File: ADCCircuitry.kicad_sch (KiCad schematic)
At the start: 16 parts, among them U7 ADS112C04

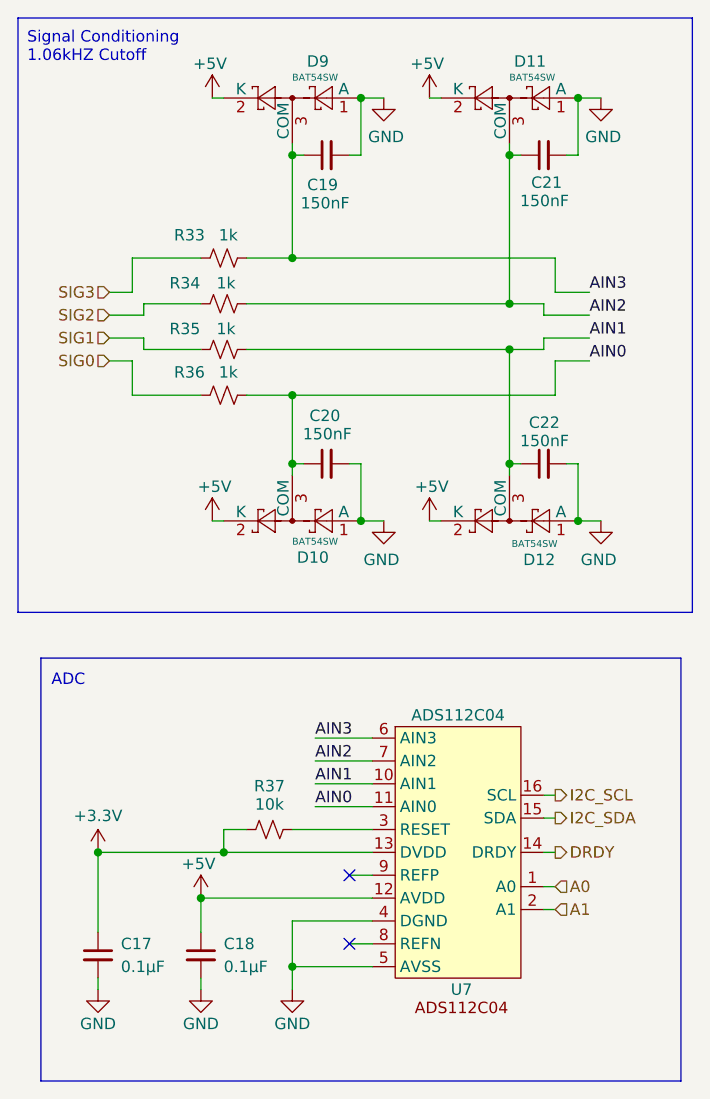
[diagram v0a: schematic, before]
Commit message: add capacitor and resistor footprints
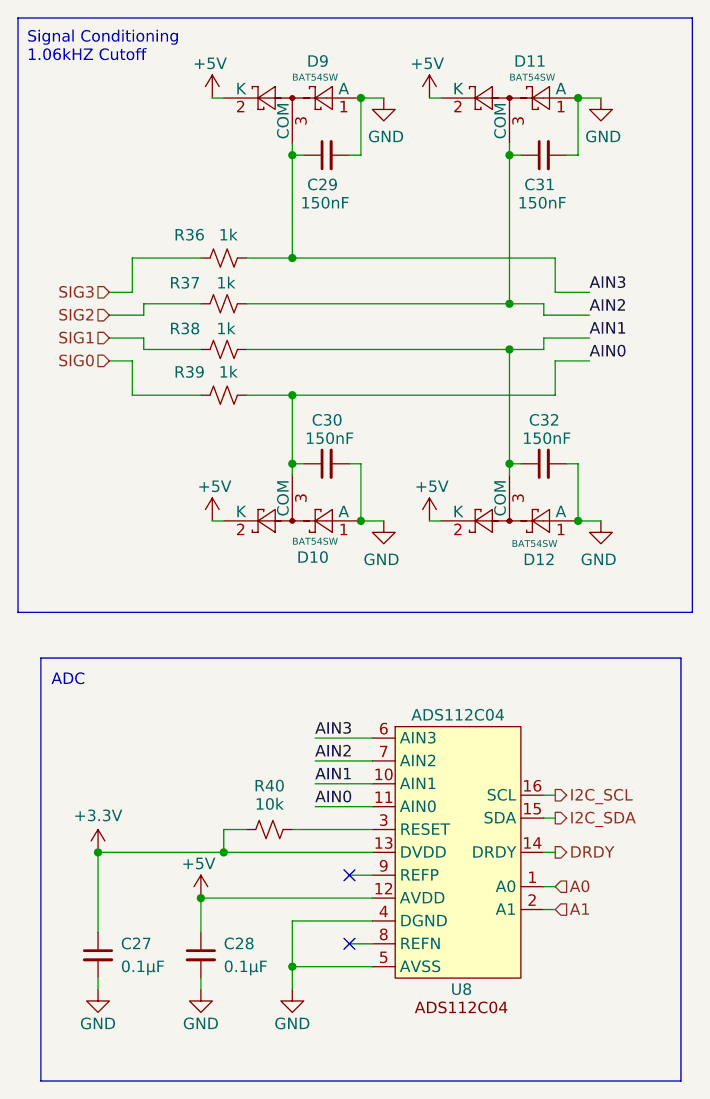
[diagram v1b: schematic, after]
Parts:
- removed C20, C21, C22: 150nF, Capacitor_SMD:C_0805_2012Metric, symbol Device:C_Small
- added C30, C31, C32: 150nF, Capacitor_SMD:C_0402_1005Metric, symbol Device:C_Small
- C27: renamed from C17; LCSC C1525 -> C307331
- C28: renamed from C18; LCSC C1525 -> C307331
- C29: renamed from C19; footprint Capacitor_SMD:C_0805_2012Metric -> Capacitor_SMD:C_0402_1005Metric; LCSC (none) -> C576725
- D10, D11, D12, D9: LCSC (none) -> C83575
- U8: renamed from U7; ADC Number 1 -> (none); I2C Address 100 0000 -> (none)
- renumbered R33 to R36, R34 to R37, R35 to R38, R36 to R39, R37 to R40
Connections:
- net AIN0: now also C30.1
- net AIN1: now also C32.1
- net AIN2: now also C31.1
- net GND: now also C30.2, C31.2, C32.2

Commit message: change clamping resistors on tc adcs for lower leakage current
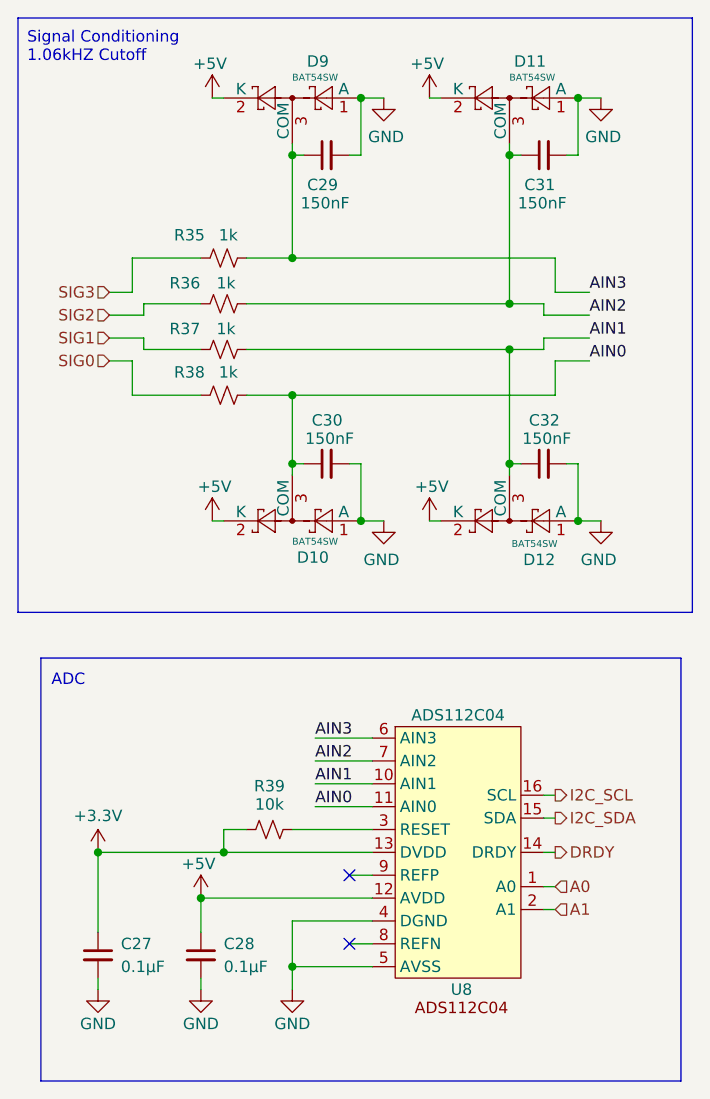
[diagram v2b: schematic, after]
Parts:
- renumbered R36 to R35, R37 to R36, R38 to R37, R39 to R38, R40 to R39
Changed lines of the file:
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@@
 		(on_board yes)
 		(dnp no)
-		(property "Reference" "#PWR076"
+		(property "Reference" "#PWR077"
 			(at 91.44 142.24 0)
 			(effects
@@
 			(project ""
 				(path "/226c5870-4123-4efa-a2b3-b42d02f59bb7/21243b6d-fc9e-4696-b2f4-96a9d8b17f22"
-					(reference "#PWR076")
+					(reference "#PWR077")
 					(unit 1)
 				)
 				(path "/226c5870-4123-4efa-a2b3-b42d02f59bb7/9fd37374-7aca-4a37-87e2-a832abf7a3a9"
-					(reference "#PWR089")
+					(reference "#PWR090")
 					(unit 1)
 				)
@@
 		(on_board yes)
 		(dnp no)
-		(property "Reference" "#PWR080"
+		(property "Reference" "#PWR081"
 			(at 104.14 87.63 0)
 			(effects
@@
 			(project "panda"
 				(path "/226c5870-4123-4efa-a2b3-b42d02f59bb7/21243b6d-fc9e-4696-b2f4-96a9d8b17f22"
-					(reference "#PWR080")
+					(reference "#PWR081")
 					(unit 1)
 				)
 				(path "/226c5870-4123-4efa-a2b3-b42d02f59bb7/9fd37374-7aca-4a37-87e2-a832abf7a3a9"
-					(reference "#PWR093")
+					(reference "#PWR094")
 					(unit 1)
 				)
@@
 		(on_board yes)
 		(dnp no)
-		(property "Reference" "#PWR083"
+		(property "Reference" "#PWR084"
 			(at 123.19 90.17 0)
 			(effects
@@
 			(project "panda"
 				(path "/226c5870-4123-4efa-a2b3-b42d02f59bb7/21243b6d-fc9e-4696-b2f4-96a9d8b17f22"
-					(reference "#PWR083")
+					(reference "#PWR084")
 					(unit 1)
 				)
 				(path "/226c5870-4123-4efa-a2b3-b42d02f59bb7/9fd37374-7aca-4a37-87e2-a832abf7a3a9"
-					(reference "#PWR096")
+					(reference "#PWR097")
 					(unit 1)
 				)
@@
 		(on_board yes)
 		(dnp no)
-		(property "Reference" "#PWR079"
+		(property "Reference" "#PWR080"
 			(at 104.14 40.64 0)
 			(effects
@@
 			(project "panda"
 				(path "/226c5870-4123-4efa-a2b3-b42d02f59bb7/21243b6d-fc9e-4696-b2f4-96a9d8b17f22"
-					(reference "#PWR079")
+					(reference "#PWR080")
 					(unit 1)
 				)
 				(path "/226c5870-4123-4efa-a2b3-b42d02f59bb7/9fd37374-7aca-4a37-87e2-a832abf7a3a9"
-					(reference "#PWR092")
+					(reference "#PWR093")
 					(unit 1)
 				)
@@
 		(on_board yes)
 		(dnp no)
-		(property "Reference" "#PWR077"
+		(property "Reference" "#PWR078"
 			(at 102.87 129.54 0)
 			(effects
@@
 			(project ""
 				(path "/226c5870-4123-4efa-a2b3-b42d02f59bb7/21243b6d-fc9e-4696-b2f4-96a9d8b17f22"
-					(reference "#PWR077")
+					(reference "#PWR078")
 					(unit 1)
 				)
 				(path "/226c5870-4123-4efa-a2b3-b42d02f59bb7/9fd37374-7aca-4a37-87e2-a832abf7a3a9"
-					(reference "#PWR090")
+					(reference "#PWR091")
 					(unit 1)
 				)
@@
 		(on_board yes)
 		(dnp no)
-		(property "Reference" "R40"
+		(property "Reference" "R39"
 			(at 110.49 113.284 90)
 			(effects
@@
 			(project ""
 				(path "/226c5870-4123-4efa-a2b3-b42d02f59bb7/21243b6d-fc9e-4696-b2f4-96a9d8b17f22"
-					(reference "R40")
+					(reference "R39")
 					(unit 1)
 				)
 				(path "/226c5870-4123-4efa-a2b3-b42d02f59bb7/9fd37374-7aca-4a37-87e2-a832abf7a3a9"
-					(reference "R45")
+					(reference "R44")
 					(unit 1)
 				)
@@
 		(on_board yes)
 		(dnp no)
-		(property "Reference" "R38"
+		(property "Reference" "R37"
 			(at 101.092 62.484 90)
 			(effects
@@
 			(project "panda"
 				(path "/226c5870-4123-4efa-a2b3-b42d02f59bb7/21243b6d-fc9e-4696-b2f4-96a9d8b17f22"
-					(reference "R38")
+					(reference "R37")
 					(unit 1)
 				)
 				(path "/226c5870-4123-4efa-a2b3-b42d02f59bb7/9fd37374-7aca-4a37-87e2-a832abf7a3a9"
-					(reference "R43")
+					(reference "R42")
 					(unit 1)
 				)
@@
 		(on_board yes)
 		(dnp no)
-		(property "Reference" "R36"
+		(property "Reference" "R35"
 			(at 101.6 52.07 90)
 			(effects
@@
 			(project "panda"
 				(path "/226c5870-4123-4efa-a2b3-b42d02f59bb7/21243b6d-fc9e-4696-b2f4-96a9d8b17f22"
-					(reference "R36")
+					(reference "R35")
 					(unit 1)
 				)
 				(path "/226c5870-4123-4efa-a2b3-b42d02f59bb7/9fd37374-7aca-4a37-87e2-a832abf7a3a9"
-					(reference "R41")
+					(reference "R40")
 					(unit 1)
 				)
@@
 		(on_board yes)
 		(dnp no)
-		(property "Reference" "#PWR078"
+		(property "Reference" "#PWR079"
 			(at 102.87 142.24 0)
 			(effects
@@
 			(project ""
 				(path "/226c5870-4123-4efa-a2b3-b42d02f59bb7/21243b6d-fc9e-4696-b2f4-96a9d8b17f22"
-					(reference "#PWR078")
+					(reference "#PWR079")
 					(unit 1)
 				)
 				(path "/226c5870-4123-4efa-a2b3-b42d02f59bb7/9fd37374-7aca-4a37-87e2-a832abf7a3a9"
-					(reference "#PWR091")
+					(reference "#PWR092")
 					(unit 1)
 				)
@@
 		(on_board yes)
 		(dnp no)
-		(property "Reference" "#PWR086"
+		(property "Reference" "#PWR087"
 			(at 147.32 43.18 0)
 			(effects
@@
 			(project "panda"
 				(path "/226c5870-4123-4efa-a2b3-b42d02f59bb7/21243b6d-fc9e-4696-b2f4-96a9d8b17f22"
-					(reference "#PWR086")
+					(reference "#PWR087")
 					(unit 1)
 				)
 				(path "/226c5870-4123-4efa-a2b3-b42d02f59bb7/9fd37374-7aca-4a37-87e2-a832abf7a3a9"
-					(reference "#PWR099")
+					(reference "#PWR0100")
 					(unit 1)
 				)
@@
 		(on_board yes)
 		(dnp no)
-		(property "Reference" "R39"
+		(property "Reference" "R38"
 			(at 101.6 67.31 90)
 			(effects
@@
 			(project "panda"
 				(path "/226c5870-4123-4efa-a2b3-b42d02f59bb7/21243b6d-fc9e-4696-b2f4-96a9d8b17f22"
-					(reference "R39")
+					(reference "R38")
 					(unit 1)
 				)
 				(path "/226c5870-4123-4efa-a2b3-b42d02f59bb7/9fd37374-7aca-4a37-87e2-a832abf7a3a9"
-					(reference "R44")
+					(reference "R43")
 					(unit 1)
 				)
@@
 		(on_board yes)
 		(dnp no)
-		(property "Reference" "#PWR075"
+		(property "Reference" "#PWR076"
 			(at 91.44 124.46 0)
 			(effects
@@
 			(project ""
 				(path "/226c5870-4123-4efa-a2b3-b42d02f59bb7/21243b6d-fc9e-4696-b2f4-96a9d8b17f22"
-					(reference "#PWR075")
+					(reference "#PWR076")
 					(unit 1)
 				)
 				(path "/226c5870-4123-4efa-a2b3-b42d02f59bb7/9fd37374-7aca-4a37-87e2-a832abf7a3a9"
-					(reference "#PWR088")
+					(reference "#PWR089")
 					(unit 1)
 				)
@@
 		(on_board yes)
 		(dnp no)
-		(property "Reference" "#PWR085"
+		(property "Reference" "#PWR086"
 			(at 128.27 87.63 0)
 			(effects
@@
 			(project "panda"
 				(path "/226c5870-4123-4efa-a2b3-b42d02f59bb7/21243b6d-fc9e-4696-b2f4-96a9d8b17f22"
-					(reference "#PWR085")
+					(reference "#PWR086")
 					(unit 1)
 				)
 				(path "/226c5870-4123-4efa-a2b3-b42d02f59bb7/9fd37374-7aca-4a37-87e2-a832abf7a3a9"
-					(reference "#PWR098")
+					(reference "#PWR099")
 					(unit 1)
 				)
@@
 		(on_board yes)
 		(dnp no)
-		(property "Reference" "#PWR084"
+		(property "Reference" "#PWR085"
 			(at 128.27 40.64 0)
 			(effects
@@
 			(project "panda"
 				(path "/226c5870-4123-4efa-a2b3-b42d02f59bb7/21243b6d-fc9e-4696-b2f4-96a9d8b17f22"
-					(reference "#PWR084")
+					(reference "#PWR085")
 					(unit 1)
 				)
 				(path "/226c5870-4123-4efa-a2b3-b42d02f59bb7/9fd37374-7aca-4a37-87e2-a832abf7a3a9"
-					(reference "#PWR097")
+					(reference "#PWR098")
 					(unit 1)
 				)
@@
 		(on_board yes)
 		(dnp no)
-		(property "Reference" "#PWR087"
+		(property "Reference" "#PWR088"
 			(at 147.32 90.17 0)
 			(effects
@@
 			(project "panda"
 				(path "/226c5870-4123-4efa-a2b3-b42d02f59bb7/21243b6d-fc9e-4696-b2f4-96a9d8b17f22"
-					(reference "#PWR087")
+					(reference "#PWR088")
 					(unit 1)
 				)
 				(path "/226c5870-4123-4efa-a2b3-b42d02f59bb7/9fd37374-7aca-4a37-87e2-a832abf7a3a9"
-					(reference "#PWR0100")
+					(reference "#PWR0101")
 					(unit 1)
 				)
@@
 		(on_board yes)
 		(dnp no)
-		(property "Reference" "#PWR081"
+		(property "Reference" "#PWR082"
 			(at 113.03 142.24 0)
 			(effects
@@
 			(project ""
 				(path "/226c5870-4123-4efa-a2b3-b42d02f59bb7/21243b6d-fc9e-4696-b2f4-96a9d8b17f22"
-					(reference "#PWR081")
+					(reference "#PWR082")
 					(unit 1)
 				)
 				(path "/226c5870-4123-4efa-a2b3-b42d02f59bb7/9fd37374-7aca-4a37-87e2-a832abf7a3a9"
-					(reference "#PWR094")
+					(reference "#PWR095")
 					(unit 1)
 				)
@@
 		(on_board yes)
 		(dnp no)
-		(property "Reference" "R37"
+		(property "Reference" "R36"
 			(at 101.092 57.404 90)
 			(effects
@@
 			(project "panda"
 				(path "/226c5870-4123-4efa-a2b3-b42d02f59bb7/21243b6d-fc9e-4696-b2f4-96a9d8b17f22"
-					(reference "R37")
+					(reference "R36")
 					(unit 1)
 				)
 				(path "/226c5870-4123-4efa-a2b3-b42d02f59bb7/9fd37374-7aca-4a37-87e2-a832abf7a3a9"
-					(reference "R42")
+					(reference "R41")
 					(unit 1)
 				)
@@
 		(on_board yes)
 		(dnp no)
-		(property "Reference" "#PWR082"
+		(property "Reference" "#PWR083"
 			(at 123.19 43.18 0)
 			(effects
@@
 			(project "panda"
 				(path "/226c5870-4123-4efa-a2b3-b42d02f59bb7/21243b6d-fc9e-4696-b2f4-96a9d8b17f22"
-					(reference "#PWR082")
+					(reference "#PWR083")
 					(unit 1)
 				)
 				(path "/226c5870-4123-4efa-a2b3-b42d02f59bb7/9fd37374-7aca-4a37-87e2-a832abf7a3a9"
-					(reference "#PWR095")
-					(unit 1)
-				)
+					(reference "#PWR096")
+					(unit 1)
+				)

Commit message: Update version number in KiCad files
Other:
- title: (none) -> PANDA
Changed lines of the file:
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@@
 	(paper "A4")
 	(title_block
-		(rev "1.0.0")
+		(title "PANDA")
+		(date "2025-12-21")
+		(rev "3.0.0")
 		(company "Queen's Rocket Engineering Team")
 	)
